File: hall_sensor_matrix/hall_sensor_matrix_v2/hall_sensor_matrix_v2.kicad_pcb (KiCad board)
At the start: 2 copper layers, 60 parts, among them J1 CTRL, J2 COL, J3 ROW, Q1 VP3203, Q2 VP3203, Q3 VP3203, Q4 VP3203, Q5 VP3203, Q6 VP3203, Q7 VP3203, Q8 VP3203, U1 74LS595, U2 74LS597, U3 74LS597

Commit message: added v2
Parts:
- added D10: LED, LED_SMD:LED_0603_1608Metric_Pad1.05x0.95mm_HandSolder, F.Cu at (142.0, 88.5)
- added D11: LED, LED_SMD:LED_0603_1608Metric_Pad1.05x0.95mm_HandSolder, F.Cu at (139.5, 88.5)
- added D12: LED, LED_SMD:LED_0603_1608Metric_Pad1.05x0.95mm_HandSolder, F.Cu at (136.9, 88.5)
- added D13: LED, LED_SMD:LED_0603_1608Metric_Pad1.05x0.95mm_HandSolder, F.Cu at (134.4, 88.5)
- added D14: LED, LED_SMD:LED_0603_1608Metric_Pad1.05x0.95mm_HandSolder, F.Cu at (131.9, 88.5)
- added D15: LED, LED_SMD:LED_0603_1608Metric_Pad1.05x0.95mm_HandSolder, F.Cu at (129.3, 88.5)
- added D16: LED, LED_SMD:LED_0603_1608Metric_Pad1.05x0.95mm_HandSolder, F.Cu at (126.8, 88.5)
- added D17: LED, LED_SMD:LED_0603_1608Metric_Pad1.05x0.95mm_HandSolder, F.Cu at (124.2, 88.5)
- added D18: LED, LED_SMD:LED_0603_1608Metric_Pad1.05x0.95mm_HandSolder, F.Cu at (121.7, 88.5)
- added D19: LED, LED_SMD:LED_0603_1608Metric_Pad1.05x0.95mm_HandSolder, F.Cu at (119.2, 88.5)
- added D20: LED, LED_SMD:LED_0603_1608Metric_Pad1.05x0.95mm_HandSolder, F.Cu at (116.6, 88.5)
- added D21: LED, LED_SMD:LED_0603_1608Metric_Pad1.05x0.95mm_HandSolder, F.Cu at (114.1, 88.5)
- added D22: LED, LED_SMD:LED_0603_1608Metric_Pad1.05x0.95mm_HandSolder, F.Cu at (111.5, 88.5)
- added D23: LED, LED_SMD:LED_0603_1608Metric_Pad1.05x0.95mm_HandSolder, F.Cu at (109.0, 88.5)
- added D24: LED, LED_SMD:LED_0603_1608Metric_Pad1.05x0.95mm_HandSolder, F.Cu at (106.4, 88.5)
- added D9: LED, LED_SMD:LED_0603_1608Metric_Pad1.05x0.95mm_HandSolder, F.Cu at (144.6, 88.5)
- added R33: 470, Resistor_SMD:R_0805_2012Metric, B.Cu at (144.6, 89.1)
- added R34: 470, Resistor_SMD:R_0805_2012Metric, B.Cu at (142.0, 89.1)
- added R35: 470, Resistor_SMD:R_0805_2012Metric, B.Cu at (139.5, 89.1)
- added R36: 470, Resistor_SMD:R_0805_2012Metric, B.Cu at (136.9, 89.1)
- added R37: 470, Resistor_SMD:R_0805_2012Metric, B.Cu at (134.4, 89.1)
- added R38: 470, Resistor_SMD:R_0805_2012Metric, B.Cu at (131.9, 89.1)
- added R39: 470, Resistor_SMD:R_0805_2012Metric, B.Cu at (129.3, 89.1)
- added R40: 470, Resistor_SMD:R_0805_2012Metric, B.Cu at (126.8, 89.1)
- added R41: 470, Resistor_SMD:R_0805_2012Metric, B.Cu at (124.2, 89.1)
- added R42: 470, Resistor_SMD:R_0805_2012Metric, B.Cu at (121.7, 89.1)
- added R43: 470, Resistor_SMD:R_0805_2012Metric, B.Cu at (119.2, 89.1)
- added R44: 470, Resistor_SMD:R_0805_2012Metric, B.Cu at (116.6, 89.1)
- added R45: 470, Resistor_SMD:R_0805_2012Metric, B.Cu at (114.1, 89.1)
- added R46: 470, Resistor_SMD:R_0805_2012Metric, B.Cu at (111.6, 89.1)
- added R47: 470, Resistor_SMD:R_0805_2012Metric, B.Cu at (109.0, 89.1)
- added R48: 470, Resistor_SMD:R_0805_2012Metric, B.Cu at (106.5, 89.1)
- moved J3 56.3 mm to (144.6, 92.3), turned to -90 degrees
- moved R17 55.7 mm to (145.2, 99.9), turned to 90 degrees
- moved U2 52.6 mm to (142.6, 96.4), turned to -90 degrees
- moved R18 52.1 mm to (142.7, 99.9), turned to 90 degrees
- moved R19 48.6 mm to (140.1, 99.9), turned to 90 degrees
- moved C2 46.4 mm to (77.9, 101.2), turned to 90 degrees
- moved R20 45.0 mm to (137.6, 99.9), turned to 90 degrees
- moved J1 43.5 mm to (75.1, 99.9), turned to 0 degrees
- moved R21 41.4 mm to (135.0, 99.9), turned to 90 degrees
- moved D8 39.7 mm to (80.9, 88.7), turned to -90 degrees
- moved R15 39.6 mm to (80.9, 88.8), turned to -90 degrees
- moved C6 38.4 mm to (79.2, 96.4), turned to 90 degrees
- moved R22 37.8 mm to (132.5, 99.9), turned to 90 degrees
- moved D7 36.5 mm to (83.5, 88.7), turned to -90 degrees
- moved R13 36.5 mm to (83.5, 88.8), turned to -90 degrees
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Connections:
- J1 pad 1: /Dout -> GND
- J1 pad 2: /Din -> +5V
- J1 pad 3: /Latch -> /Din
- J1 pad 4: /CLK -> /Latch
- J1 pad 5: +5V -> /CLK
- J1 pad 6: GND -> /Dout
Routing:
- net GND: track 62.9 -> 136.6 mm
- net /Latch: track 0.00 -> 71.1 mm, vias 0 -> 2
- net /CLK: track 0.00 -> 69.1 mm, vias 0 -> 1
- net +5V: track 125.2 -> 193.7 mm, vias 4 -> 5
- net /Dout: track 0.00 -> 39.5 mm
- net /Din: track 0.00 -> 27.6 mm
- net /R0: track 0.00 -> 24.0 mm
- net /Dout_1: track 0.00 -> 12.0 mm
- net /R8: track 7.50 -> 17.5 mm, vias 0 -> 1
- net /R4: track 6.97 -> 9.93 mm
- net /R15: track 6.97 -> 9.92 mm
- net /R5: track 6.97 -> 9.91 mm
- net /R1: track 6.97 -> 9.91 mm
- net /R7: track 6.97 -> 9.91 mm
- net /R14: track 6.97 -> 9.91 mm
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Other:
- board outline added: 74 x 31 mm
- board text added: "Hall sensor matrix X.B. 9/23 revA JLCJLCJLCJLC"

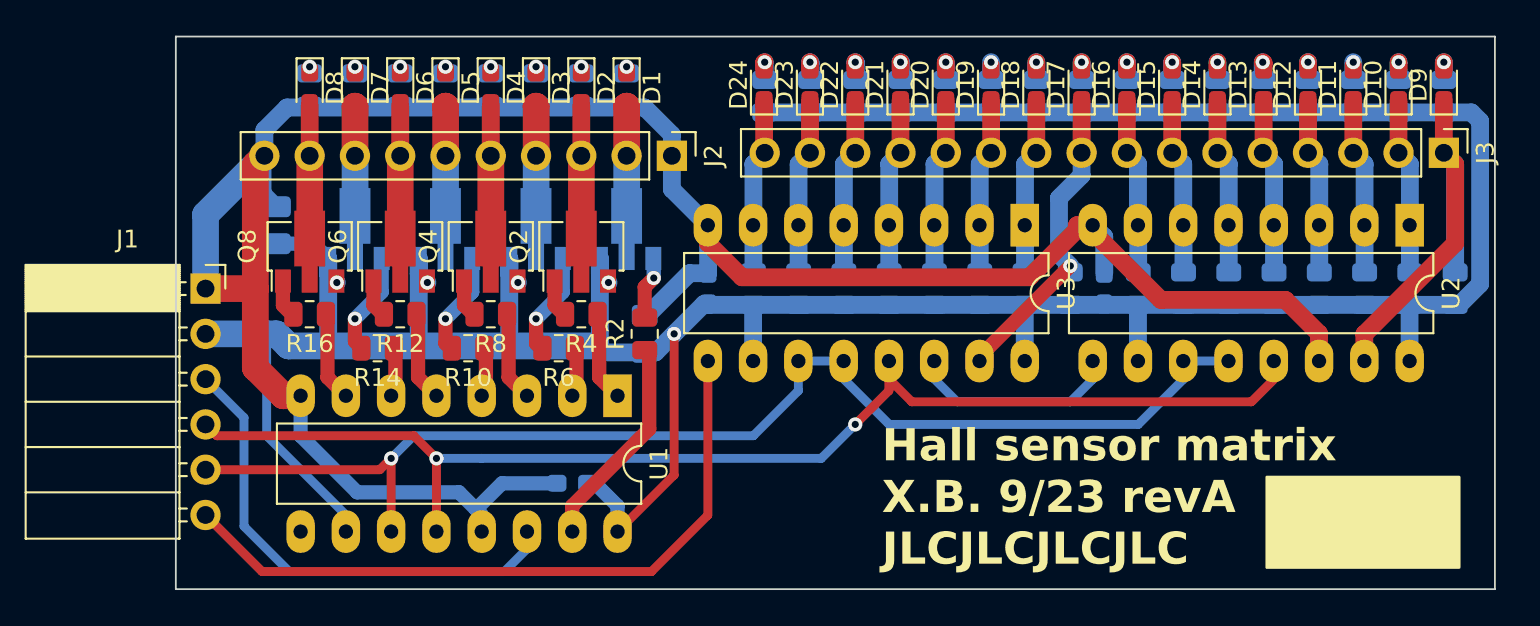
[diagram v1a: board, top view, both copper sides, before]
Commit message: added ltspice
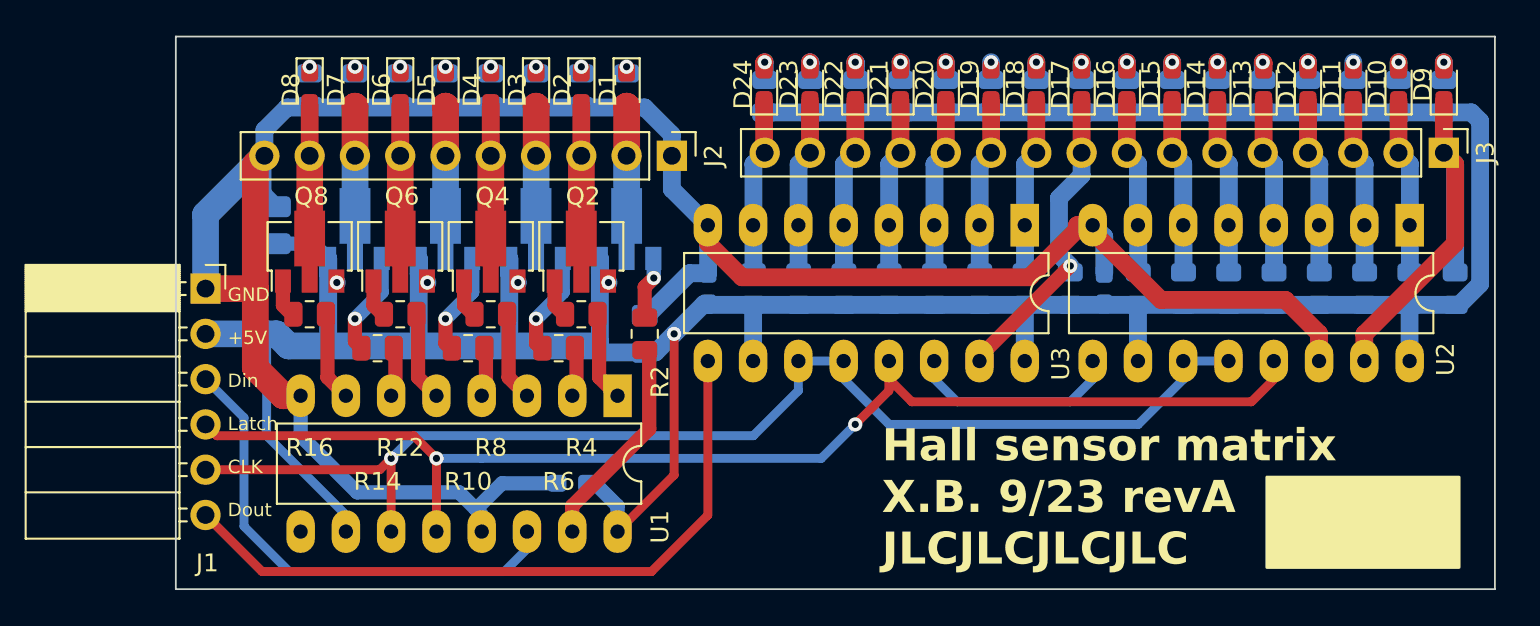
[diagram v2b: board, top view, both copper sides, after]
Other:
- board text added: "GND +5V Din Latch CLK Dout"

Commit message: added content
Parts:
- added H1: MountingHole, MountingHole:MountingHole_3.2mm_M3, F.Cu at (41.0, 63.0)
- added H2: MountingHole, MountingHole:MountingHole_3.2mm_M3, F.Cu at (111.5, 86.5)
- moved C6 42.5 mm to (46.3, 69.4)
- moved R33 42.5 mm to (111.7, 62.1)
- moved R37 42.5 mm to (101.5, 62.1)
- moved R40 42.5 mm to (93.9, 62.1)
- moved C4 42.5 mm to (66.8, 75.5)
- moved D16 42.5 mm to (93.9, 61.5)
- moved D23 42.5 mm to (76.1, 61.5)
- moved D9 42.5 mm to (111.7, 61.5)
- moved J2 42.5 mm to (68.4, 65.5)
- moved J3 42.5 mm to (111.7, 65.3)
- moved R13 42.5 mm to (50.6, 61.8)
- moved R18 42.5 mm to (109.8, 72.9)
- moved R19 42.5 mm to (107.2, 72.9)
- moved R2 42.5 mm to (66.8, 75.5)
- moved R22 42.5 mm to (99.6, 72.9)
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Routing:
- added copper zone on B.Cu, net GND
- added copper zone on F.Cu, net GND
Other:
- board size 74 x 31 mm -> 77.5 x 30.5 mm
- board text added: "1"
- board text added: "2"
